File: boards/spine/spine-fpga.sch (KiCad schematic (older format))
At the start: 29 parts, among them U7 iCE40-HX1K-TQ144

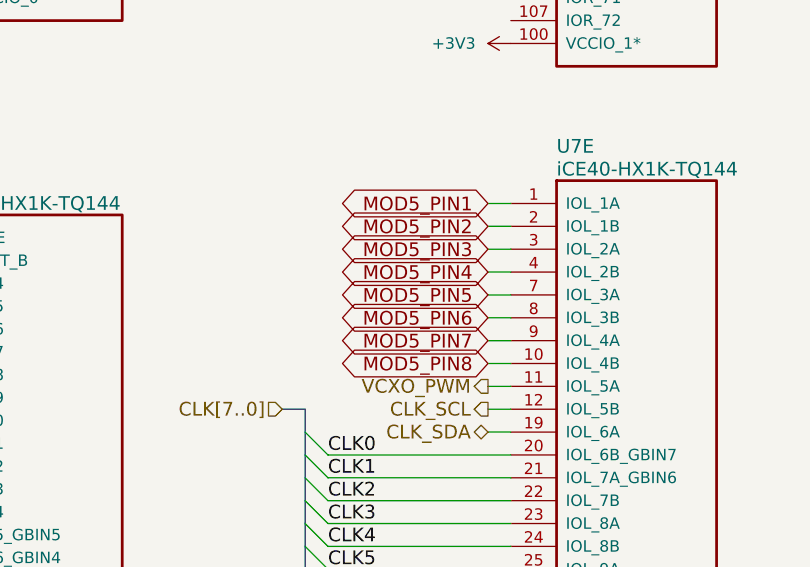
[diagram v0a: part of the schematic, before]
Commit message: Starting module routing
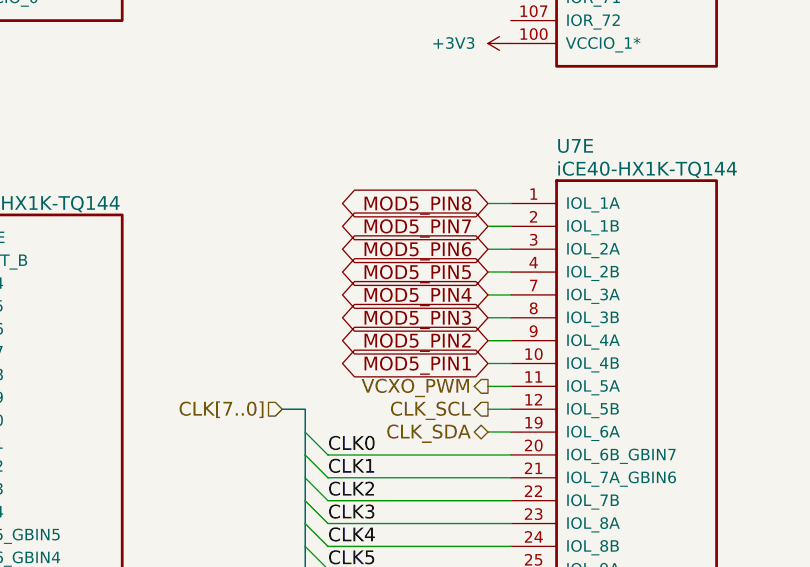
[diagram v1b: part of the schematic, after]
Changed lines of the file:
@@
 Text GLabel 14250 7050 0    60   BiDi ~ 0
 MOD4_PIN8
-Text GLabel 9050 4100 0    60   BiDi ~ 0
+Text GLabel 9050 4800 0    60   BiDi ~ 0
 MOD5_PIN1
-Text GLabel 9050 4200 0    60   BiDi ~ 0
+Text GLabel 9050 4700 0    60   BiDi ~ 0
 MOD5_PIN2
-Text GLabel 9050 4300 0    60   BiDi ~ 0
+Text GLabel 9050 4600 0    60   BiDi ~ 0
 MOD5_PIN3
-Text GLabel 9050 4500 0    60   BiDi ~ 0
+Text GLabel 9050 4400 0    60   BiDi ~ 0
 MOD5_PIN5
-Text GLabel 9050 4700 0    60   BiDi ~ 0
+Text GLabel 9050 4200 0    60   BiDi ~ 0
 MOD5_PIN7
-Text GLabel 9050 4400 0    60   BiDi ~ 0
+Text GLabel 9050 4500 0    60   BiDi ~ 0
 MOD5_PIN4
-Text GLabel 9050 4600 0    60   BiDi ~ 0
+Text GLabel 9050 4300 0    60   BiDi ~ 0
 MOD5_PIN6
-Text GLabel 9050 4800 0    60   BiDi ~ 0
+Text GLabel 9050 4100 0    60   BiDi ~ 0
 MOD5_PIN8
 Text GLabel 12150 5100 0    60   BiDi ~ 0
@@
 FB 59 00 E6 A5 69 3A 37 9E CF 73 BC F7 37 E3 33 5D 9E A8 3E 7F 80 FA F7 F6 BB 44 F4 6E D4 E7 77
 A2 1E 1F 27 A2 E3 16 70 32 E9 54 FE 3F E7 AF 00 CA 1C A3 36 0A 00 00 00 00 49 45 4E 44 AE 42 60
-82 FF
+82 70
 EndData
 $EndBitmap
@@
 FB 59 00 E6 A5 69 3A 37 9E CF 73 BC F7 37 E3 33 5D 9E A8 3E 7F 80 FA F7 F6 BB 44 F4 6E D4 E7 77
 A2 1E 1F 27 A2 E3 16 70 32 E9 54 FE 3F E7 AF 00 CA 1C A3 36 0A 00 00 00 00 49 45 4E 44 AE 42 60
-82 FF
+82 00
 EndData
 $EndBitmap

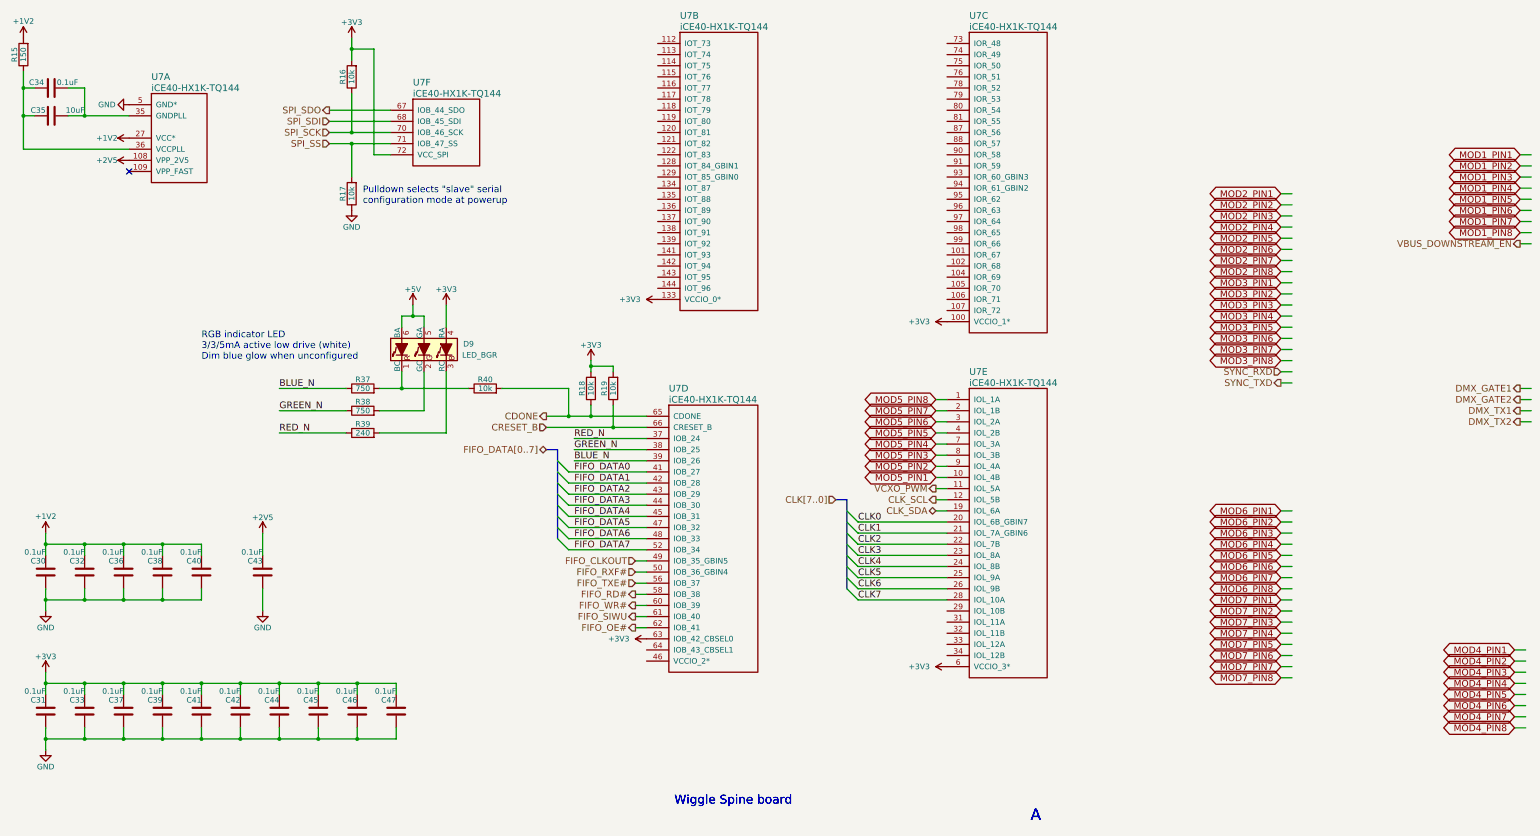
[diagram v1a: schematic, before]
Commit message: More swapping and rerouting on the FPGA
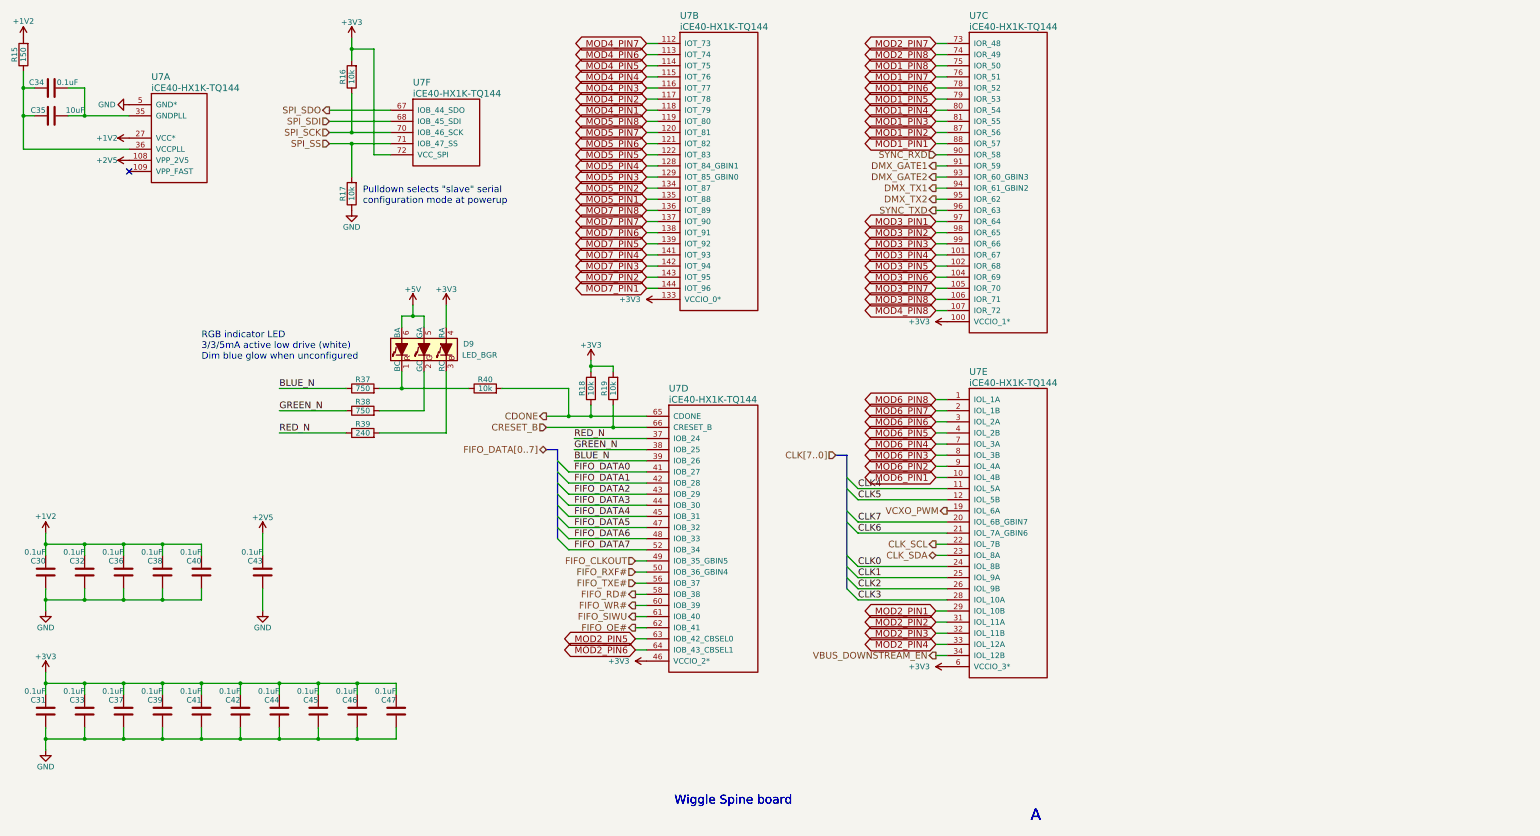
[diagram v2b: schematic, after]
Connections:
- wire segments 168 -> 167

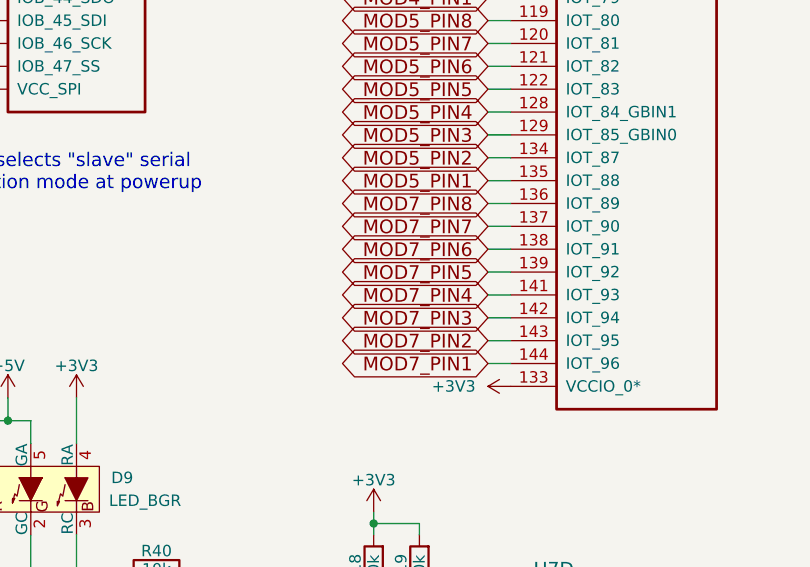
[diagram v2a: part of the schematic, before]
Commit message: Routing: GPIOs, mid-current power busses
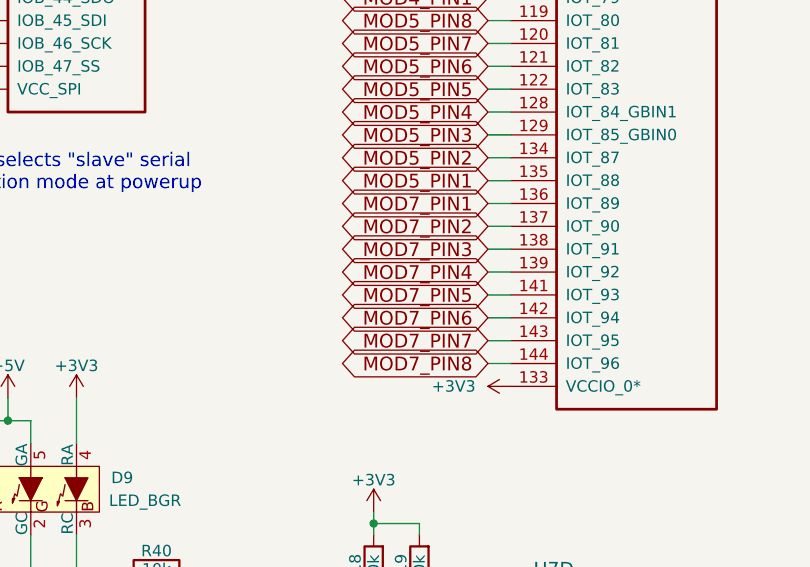
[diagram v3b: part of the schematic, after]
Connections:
- net MOD7_PIN1: now also U7.136 (IOT_89); no longer U7.144 (IOT_96)
- net MOD7_PIN2: now also U7.137 (IOT_90); no longer U7.143 (IOT_95)
- net MOD7_PIN3: now also U7.138 (IOT_91); no longer U7.142 (IOT_94)
- net MOD7_PIN4: now also U7.139 (IOT_92); no longer U7.141 (IOT_93)
- net MOD7_PIN5: now also U7.141 (IOT_93); no longer U7.139 (IOT_92)
- net MOD7_PIN6: now also U7.142 (IOT_94); no longer U7.138 (IOT_91)
- net MOD7_PIN7: now also U7.143 (IOT_95); no longer U7.137 (IOT_90)
- net MOD7_PIN8: now also U7.144 (IOT_96); no longer U7.136 (IOT_89)
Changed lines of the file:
@@
 $Comp
 L iCE40-HX1K-TQ144 U7
-U 1 1 5637E334
-P 1800 1450
-F 0 "U7" H 2000 1700 60  0000 L CNN
-F 1 "iCE40-HX1K-TQ144" H 2000 1600 60  0000 L CNN
-F 2 "Housings_QFP:TQFP-144_20x20mm_Pitch0.5mm" H 1800 1450 60  0001 C CNN
-F 3 "http://www.latticesemi.com/~/media/LatticeSemi/Documents/DataSheets/iCE/iCE40LPHXFamilyDataSheet.pdf" H 1800 1450 60  0001 C CNN
-F 4 "4.5703" H 1800 1450 60  0001 C CNN "RefPrice1k"
-F 5 "Lattice" H 1800 1450 60  0001 C CNN "MfrId"
-F 6 "ICE40HX1K-TQ144" H 1800 1450 60  0001 C CNN "MfgId"
-F 7 "220-1565-ND" H 1800 1450 60  0001 C CNN "Vend1Id"
-F 8 "Digikey" H 1800 1450 60  0001 C CNN "Vend1"
-	1    1800 1450
-	1    0    0    -1
-$EndComp
-$Comp
-L iCE40-HX1K-TQ144 U7
 U 2 1 5637E355
 P 6550 900
@@
 Text GLabel 9050 4100 0    60   BiDi ~ 0
 MOD6_PIN8
-Text GLabel 6450 3100 0    60   BiDi ~ 0
+Text GLabel 6450 2400 0    60   BiDi ~ 0
 MOD7_PIN1
-Text GLabel 6450 3000 0    60   BiDi ~ 0
+Text GLabel 6450 2500 0    60   BiDi ~ 0
 MOD7_PIN2
-Text GLabel 6450 2900 0    60   BiDi ~ 0
+Text GLabel 6450 2600 0    60   BiDi ~ 0
 MOD7_PIN3
-Text GLabel 6450 2700 0    60   BiDi ~ 0
+Text GLabel 6450 2800 0    60   BiDi ~ 0
 MOD7_PIN5
-Text GLabel 6450 2500 0    60   BiDi ~ 0
+Text GLabel 6450 3000 0    60   BiDi ~ 0
 MOD7_PIN7
-Text GLabel 6450 2800 0    60   BiDi ~ 0
+Text GLabel 6450 2700 0    60   BiDi ~ 0
 MOD7_PIN4
-Text GLabel 6450 2600 0    60   BiDi ~ 0
+Text GLabel 6450 2900 0    60   BiDi ~ 0
 MOD7_PIN6
-Text GLabel 6450 2400 0    60   BiDi ~ 0
+Text GLabel 6450 3100 0    60   BiDi ~ 0
 MOD7_PIN8
 Wire Wire Line
@@
 FB 59 00 E6 A5 69 3A 37 9E CF 73 BC F7 37 E3 33 5D 9E A8 3E 7F 80 FA F7 F6 BB 44 F4 6E D4 E7 77
 A2 1E 1F 27 A2 E3 16 70 32 E9 54 FE 3F E7 AF 00 CA 1C A3 36 0A 00 00 00 00 49 45 4E 44 AE 42 60
-82 00
+82 6E
 EndData
 $EndBitmap
@@
 72 0F 1C A9 DC 70 49 CB 79 33 88 85 99 AD 01 6C 4B 10 FC 3B 13 DE 3B 37 68 79 AD 07 BC 00 3C 0E
 3C 31 EE E3 D8 E7 0F 03 D7 7B 9F FB C1 E1 FF 01 18 C4 96 1D B8 0E 40 07 00 00 00 00 49 45 4E 44
-AE 42 60 82 A3
+AE 42 60 82 11
 EndData
 $EndBitmap
@@
 72 0F 1C A9 DC 70 49 CB 79 33 88 85 99 AD 01 6C 4B 10 FC 3B 13 DE 3B 37 68 79 AD 07 BC 00 3C 0E
 3C 31 EE E3 D8 E7 0F 03 D7 7B 9F FB C1 E1 FF 01 18 C4 96 1D B8 0E 40 07 00 00 00 00 49 45 4E 44
-AE 42 60 82 A3
+AE 42 60 82 00
 EndData
 $EndBitmap
@@
 Wire Wire Line
 	9150 5300 8350 5300
+$Comp
+L iCE40-HX1K-TQ144 U7
+U 1 1 5637E334
+P 1800 1450
+F 0 "U7" H 2000 1700 60  0000 L CNN
+F 1 "iCE40-HX1K-TQ144" H 2000 1600 60  0000 L CNN
+F 2 "Housings_QFP:TQFP-144_20x20mm_Pitch0.5mm" H 1800 1450 60  0001 C CNN
+F 3 "http://www.latticesemi.com/~/media/LatticeSemi/Documents/DataSheets/iCE/iCE40LPHXFamilyDataSheet.pdf" H 1800 1450 60  0001 C CNN
+F 4 "4.5703" H 1800 1450 60  0001 C CNN "RefPrice1k"
+F 5 "Lattice" H 1800 1450 60  0001 C CNN "MfrId"
+F 6 "ICE40HX1K-TQ144" H 1800 1450 60  0001 C CNN "MfgId"
+F 7 "220-1565-ND" H 1800 1450 60  0001 C CNN "Vend1Id"
+F 8 "Digikey" H 1800 1450 60  0001 C CNN "Vend1"
+	1    1800 1450
+	1    0    0    -1
+$EndComp
 $EndSCHEMATC

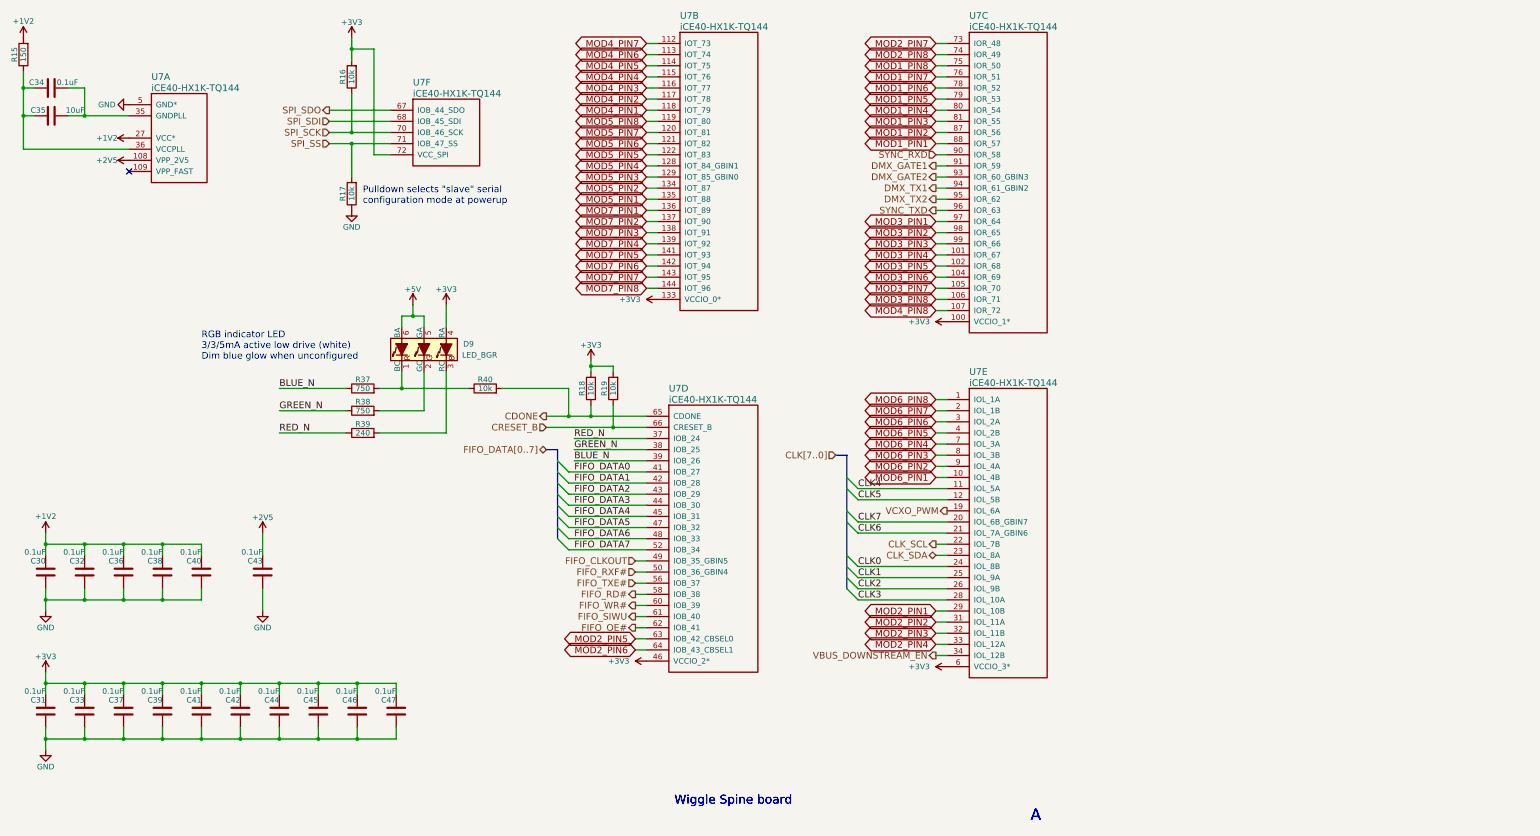
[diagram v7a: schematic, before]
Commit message: BOM cleanup
Especially fix the confusing and mostly incorrect Mfg/Mfr stuff that I inherited from somewhere.
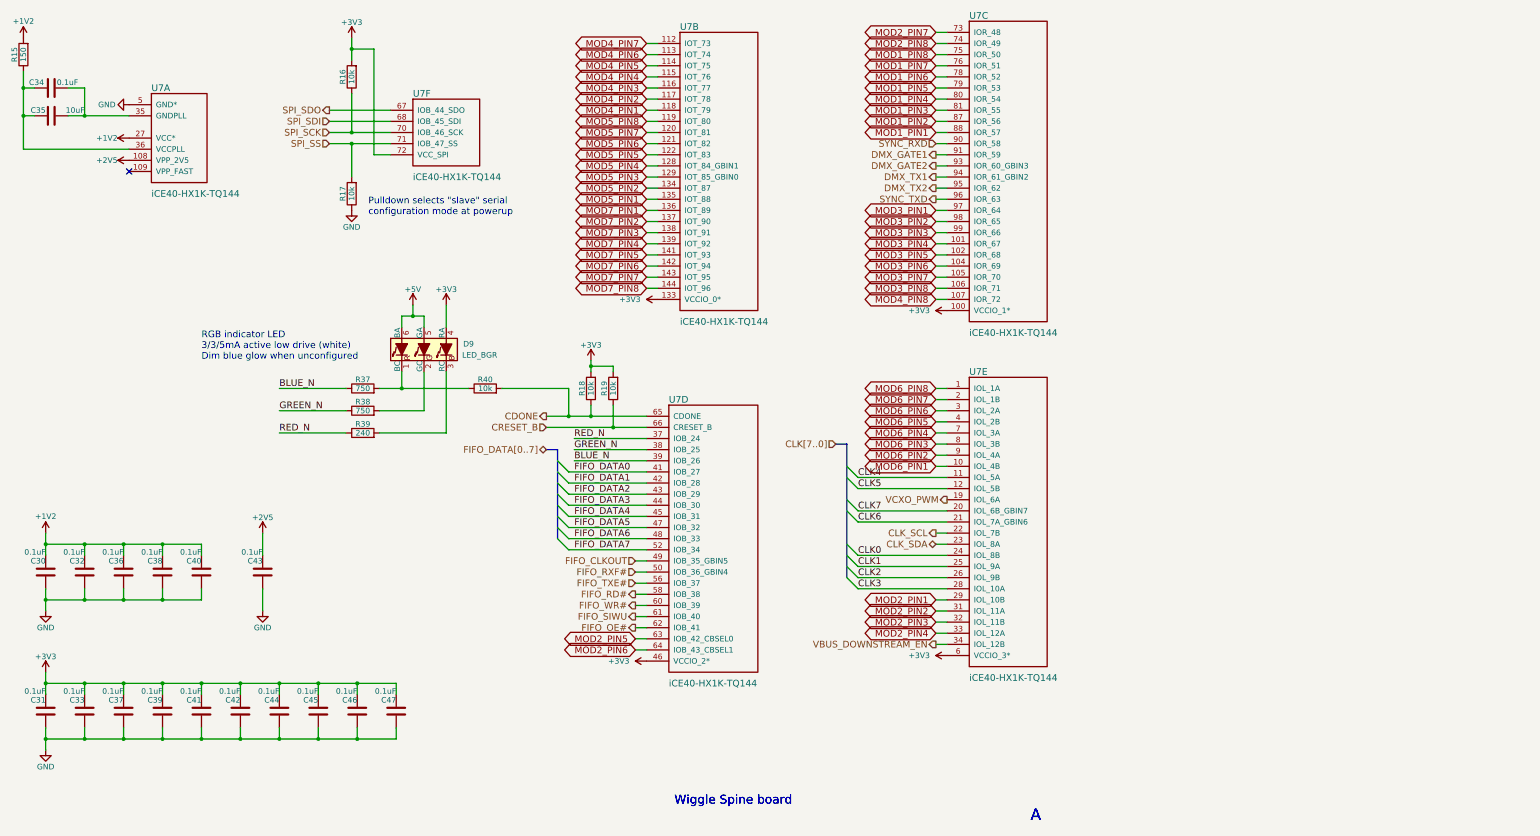
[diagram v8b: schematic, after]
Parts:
- C30, C31, C32, C33, C34, C36, C37, C38, C39, C40, C41, C42, C43, C44, C45, C46, C47: Mfg1 (none) -> Murata; Mfg1Id (none) -> GRM21BR71H104MA01L; MfgId GRM21BR71H104MA01L -> (none); MfrId Murata -> (none)
- C35: Mfg1 (none) -> Murata; Mfg1Id (none) -> GRM31CR61H106MA12L; MfgId GRM31CR61H106MA12L -> (none); MfrId Murata -> (none)
- D9: Mfg1 (none) -> Cree; Mfg1Id (none) -> CLY6D-FKC-CK1N1D1BB7D3D3; MfgId Cree -> (none); MfrId CLY6D-FKC-CK1N1D1BB7D3D3 -> (none)
- R15: Mfg1 (none) -> Stackpole; Mfg1Id (none) -> RMCF0805JT150R; MfgId RMCF0805JT150R -> (none); MfrId Stackpole -> (none)
- R16, R17, R18, R19, R40: Mfg1 (none) -> Stackpole; Mfg1Id (none) -> RMCF0805JT10K0; MfgId RMCF0805JT10K0 -> (none); MfrId Stackpole -> (none)
- R37, R38: Mfg1 (none) -> Stackpole; Mfg1Id (none) -> RMCF0805JT750R; MfgId RMCF0805JT750R -> (none); MfrId Stackpole -> (none)
- R39: Mfg1 (none) -> Stackpole; Mfg1Id (none) -> RMCF0805JT240R; MfgId RMCF0805JT240R -> (none); MfrId Stackpole -> (none)
- U7: Mfg1 (none) -> Lattice; Mfg1Id (none) -> ICE40HX1K-TQ144; MfgId ICE40HX1K-TQ144 -> (none); MfrId Lattice -> (none)
- U7: Mfg1 (none) -> Lattice; Mfg1Id (none) -> ICE40HX1K-TQ144; RefPrice1k (none) -> 4.5703; Vend1 (none) -> Digikey; Vend1Id (none) -> 220-1565-ND
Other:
- moved on the sheet: U7C, U7E
